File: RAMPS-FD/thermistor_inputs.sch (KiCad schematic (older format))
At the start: 31 parts, among them P301 THERMISTORS, U1001 TL431_SOT23_RMC

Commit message: Changed fuse holders to Keystone 3568; specificy HCT instead of ACT logic
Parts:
- D1001, D1002, D1003, D1004, D1005, D1006, D1007, D1008: footprint w_smd_diode:SOD323 -> Diodes_SMD:SOD-123; symbol DIODE -> D
- P301: footprint w_pin_strip:pin_strip_4x2 -> Pin_Headers:Pin_Header_Straight_2x04
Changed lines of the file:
@@
 F 0 "P301" H 2350 2800 50  0000 C CNN
 F 1 "THERMISTORS" V 2350 2550 40  0000 C CNN
-F 2 "w_pin_strip:pin_strip_4x2" H 2350 2550 60  0001 C CNN
+F 2 "Pin_Headers:Pin_Header_Straight_2x04" H 2350 2550 60  0001 C CNN
 F 3 "" H 2350 2550 60  0001 C CNN
 	1    2350 2550
@@
 $EndComp
 $Comp
-L DIODE D1002
+L D D1002
 U 1 1 52C438B2
 P 5050 1800
 F 0 "D1002" H 5050 1900 40  0000 C CNN
 F 1 "1N4148" H 5050 1700 40  0000 C CNN
-F 2 "w_smd_diode:SOD323" H 5050 1800 60  0001 C CNN
+F 2 "Diodes_SMD:SOD-123" H 5050 1800 60  0001 C CNN
 F 3 "~" H 5050 1800 60  0000 C CNN
 	1    5050 1800
@@
 $EndComp
 $Comp
-L DIODE D1001
+L D D1001
 U 1 1 52C43922
 P 5050 1300
 F 0 "D1001" H 5050 1400 40  0000 C CNN
 F 1 "1N4148" H 5050 1200 40  0000 C CNN
-F 2 "w_smd_diode:SOD323" H 5050 1300 60  0001 C CNN
+F 2 "Diodes_SMD:SOD-123" H 5050 1300 60  0001 C CNN
 F 3 "~" H 5050 1300 60  0000 C CNN
 	1    5050 1300
@@
 OV_REF
 $Comp
-L DIODE D1007
+L D D1007
 U 1 1 52C565E9
 P 5100 3100
 F 0 "D1007" H 5100 3200 40  0000 C CNN
 F 1 "1N4148" H 5100 3000 40  0000 C CNN
-F 2 "w_smd_diode:SOD323" H 5100 3100 60  0001 C CNN
+F 2 "Diodes_SMD:SOD-123" H 5100 3100 60  0001 C CNN
 F 3 "~" H 5100 3100 60  0000 C CNN
 	1    5100 3100
@@
 OV_REF
 $Comp
-L DIODE D1008
+L D D1008
 U 1 1 52C565F2
 P 5100 3600
 F 0 "D1008" H 5100 3700 40  0000 C CNN
 F 1 "1N4148" H 5100 3500 40  0000 C CNN
-F 2 "w_smd_diode:SOD323" H 5100 3600 60  0001 C CNN
+F 2 "Diodes_SMD:SOD-123" H 5100 3600 60  0001 C CNN
 F 3 "~" H 5100 3600 60  0000 C CNN
 	1    5100 3600
@@
 $EndComp
 $Comp
-L DIODE D1004
+L D D1004
 U 1 1 52C565F8
 P 5000 5100
 F 0 "D1004" H 5000 5200 40  0000 C CNN
 F 1 "1N4148" H 5000 5000 40  0000 C CNN
-F 2 "w_smd_diode:SOD323" H 5000 5100 60  0001 C CNN
+F 2 "Diodes_SMD:SOD-123" H 5000 5100 60  0001 C CNN
 F 3 "~" H 5000 5100 60  0000 C CNN
 	1    5000 5100
@@
 $EndComp
 $Comp
-L DIODE D1003
+L D D1003
 U 1 1 52C56608
 P 5000 4550
 F 0 "D1003" H 5000 4650 40  0000 C CNN
 F 1 "1N4148" H 5000 4450 40  0000 C CNN
-F 2 "w_smd_diode:SOD323" H 5000 4550 60  0001 C CNN
+F 2 "Diodes_SMD:SOD-123" H 5000 4550 60  0001 C CNN
 F 3 "~" H 5000 4550 60  0000 C CNN
 	1    5000 4550
@@
 OV_REF
 $Comp
-L DIODE D1005
+L D D1005
 U 1 1 52C56611
 P 5000 6100
 F 0 "D1005" H 5000 6200 40  0000 C CNN
 F 1 "1N4148" H 5000 6000 40  0000 C CNN
-F 2 "w_smd_diode:SOD323" H 5000 6100 60  0001 C CNN
+F 2 "Diodes_SMD:SOD-123" H 5000 6100 60  0001 C CNN
 F 3 "~" H 5000 6100 60  0000 C CNN
 	1    5000 6100
@@
 OV_REF
 $Comp
-L DIODE D1006
+L D D1006
 U 1 1 52C5661A
 P 5000 6700
 F 0 "D1006" H 5000 6800 40  0000 C CNN
 F 1 "1N4148" H 5000 6600 40  0000 C CNN
-F 2 "w_smd_diode:SOD323" H 5000 6700 60  0001 C CNN
+F 2 "Diodes_SMD:SOD-123" H 5000 6700 60  0001 C CNN
 F 3 "~" H 5000 6700 60  0000 C CNN
 	1    5000 6700
@@
 	8600 1950 8600 2300
 Wire Wire Line
-	5050 2050 5050 2000
+	5050 2050 5050 1950
 Connection ~ 5500 2050
 Wire Wire Line
-	5050 1500 5050 1600
+	5050 1450 5050 1650
 Connection ~ 5050 1550
 Wire Wire Line
@@
 	5350 1000 5050 1000
 Wire Wire Line
-	5050 1000 5050 1100
+	5050 1000 5050 1150
 Wire Wire Line
 	3900 1400 3900 1550
@@
 	5400 2700 5100 2700
 Wire Wire Line
-	5100 2700 5100 2900
+	5100 2700 5100 2950
 Wire Wire Line
 	5300 4250 5000 4250
 Wire Wire Line
-	5000 4250 5000 4350
+	5000 4250 5000 4400
 Wire Wire Line
 	5300 5750 5000 5750
 Wire Wire Line
-	5000 5750 5000 5900
-Wire Wire Line
-	5100 3850 5100 3800
+	5000 5750 5000 5950
+Wire Wire Line
+	5100 3850 5100 3750
 Connection ~ 5600 3850
 Wire Wire Line
-	5100 3300 5100 3400
+	5100 3250 5100 3450
 Connection ~ 5100 3350
 Wire Wire Line
@@
 Connection ~ 4000 4850
 Wire Wire Line
-	5000 4750 5000 4900
+	5000 4700 5000 4950
 Connection ~ 5000 4850
 Wire Wire Line
-	5000 5350 5000 5300
+	5000 5350 5000 5250
 Connection ~ 5600 5350
 Wire Wire Line
@@
 Connection ~ 4000 6400
 Wire Wire Line
-	5000 6300 5000 6500
+	5000 6250 5000 6550
 Connection ~ 5000 6400
 Wire Wire Line
-	5000 7000 5000 6900
+	5000 7000 5000 6850
 Connection ~ 5650 7000
 Wire Wire Line

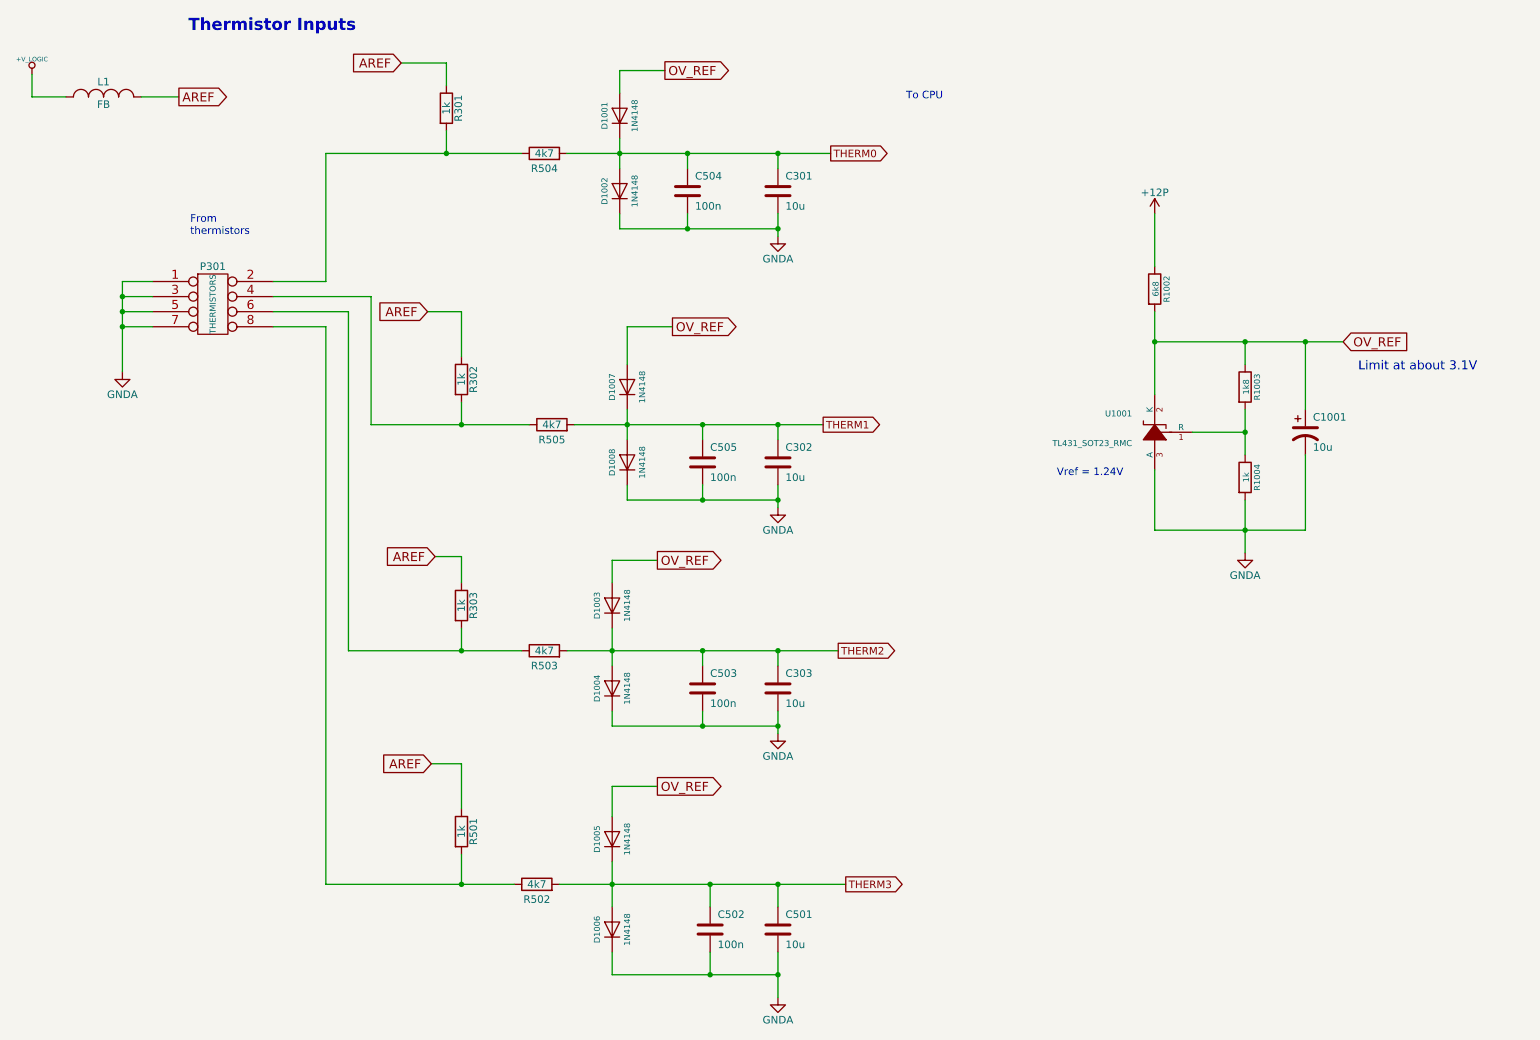
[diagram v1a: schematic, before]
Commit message: Fix 3d view; remove faulty ADC protection
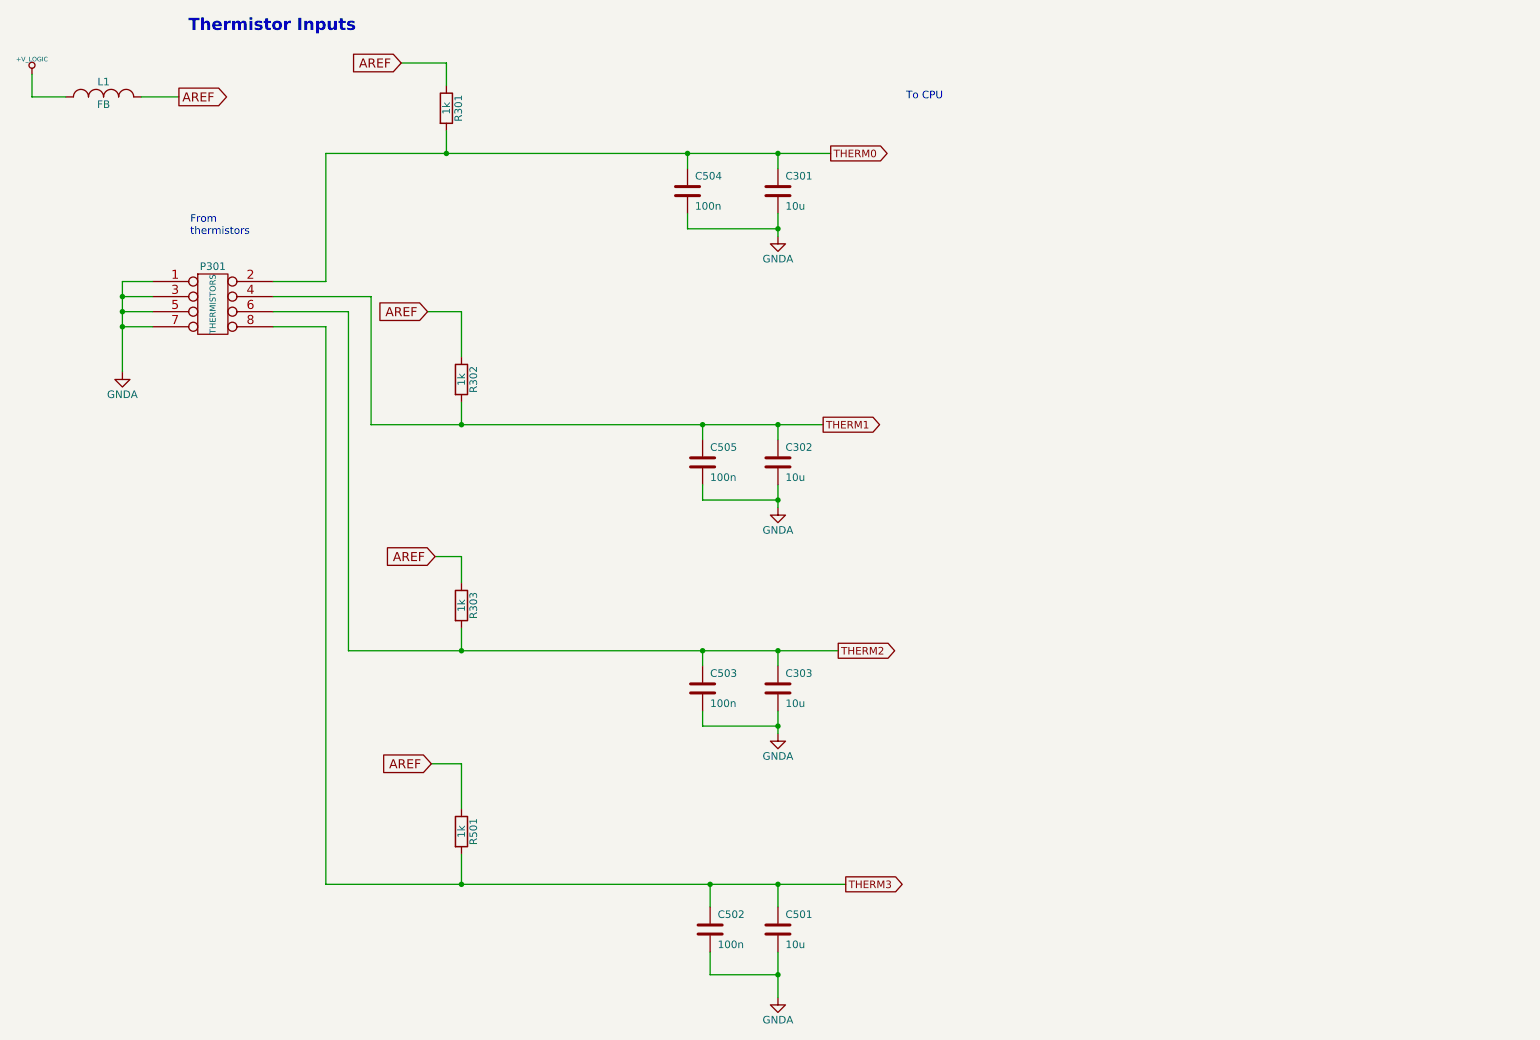
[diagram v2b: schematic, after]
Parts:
- removed C1001: 10u, Capacitors_SMD:c_elec_4x5.3, symbol CP1
- removed D1001, D1002, D1003, D1004, D1005, D1006, D1007, D1008: 1N4148, Diodes_SMD:SOD-123, symbol D
- removed R1002: 6k8, Resistors_SMD:R_0603, symbol R
- removed R1003: 1k8, Resistors_SMD:R_0603, symbol R
- removed R1004: 1k, Resistors_SMD:R_0603, symbol R
- removed R502, R503, R504, R505: 4k7, Resistors_SMD:R_0603, symbol R
- removed U1001: TL431_SOT23_RMC, libcms:SOT23, symbol TL431_SOT23_RMC
- P301: footprint Pin_Headers:Pin_Header_Straight_2x04 -> Pin_Headers:Pin_Header_Straight_2x04_Pitch2.54mm
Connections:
- net THERM0: now also P301.2, R301.2
- net THERM1: now also P301.4, R302.2
- net THERM2: now also P301.6, R303.2
- net THERM3: now also P301.8, R501.2
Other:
- note removed: "Limit at about 3.1V"
- note removed: "Vref = 1.24V"
